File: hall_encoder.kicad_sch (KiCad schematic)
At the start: 30 parts, among them J1 Conn_02x03_Odd_Even, J2 Conn_01x04, J3 Conn_01x04, J4 Conn_01x02, J5 Conn_01x02, J6 Conn_01x02, SW1 RESET, U1 AP2210, U2 STM32F042F4Px, U3 MA730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

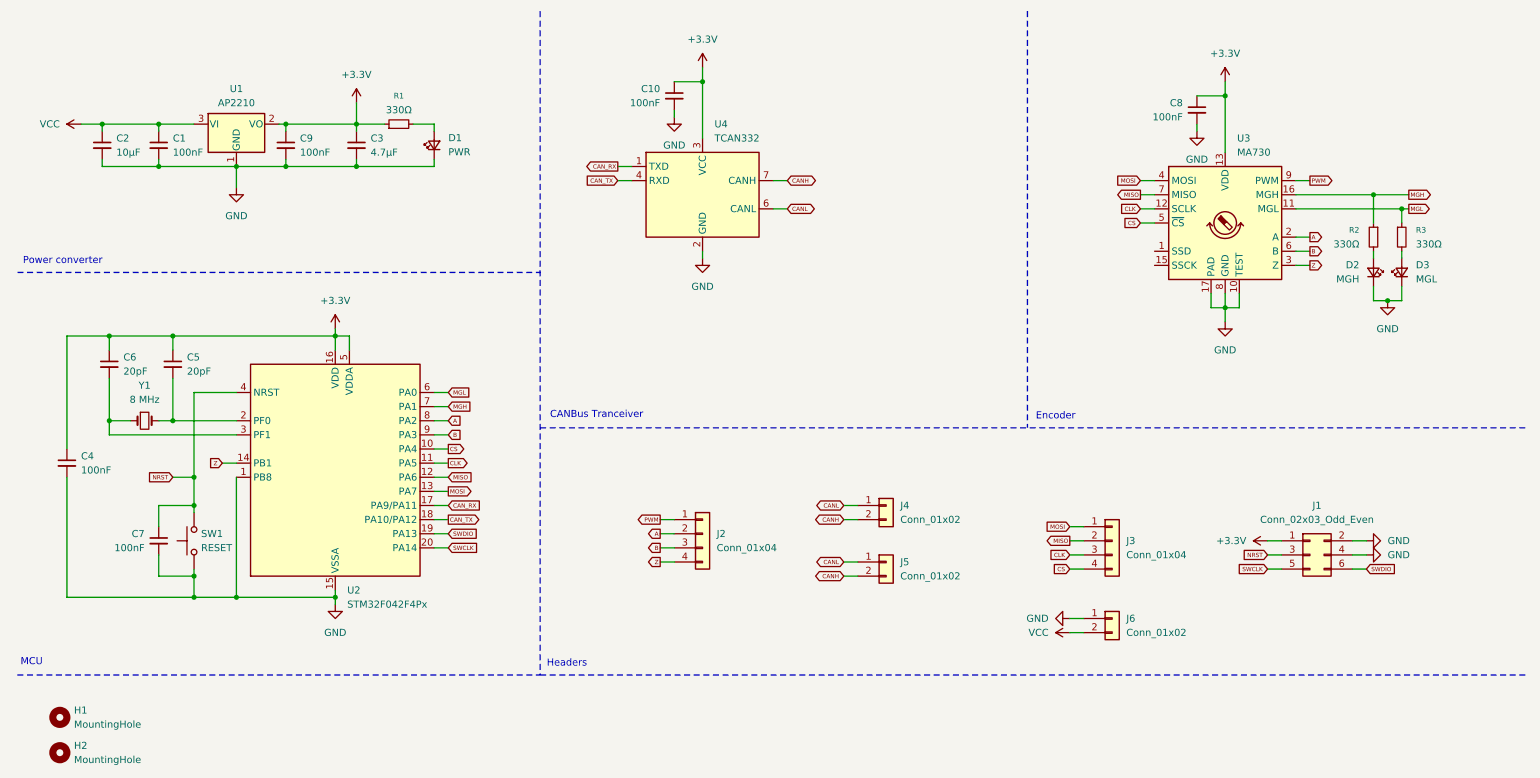
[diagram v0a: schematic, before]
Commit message: Remove all can components
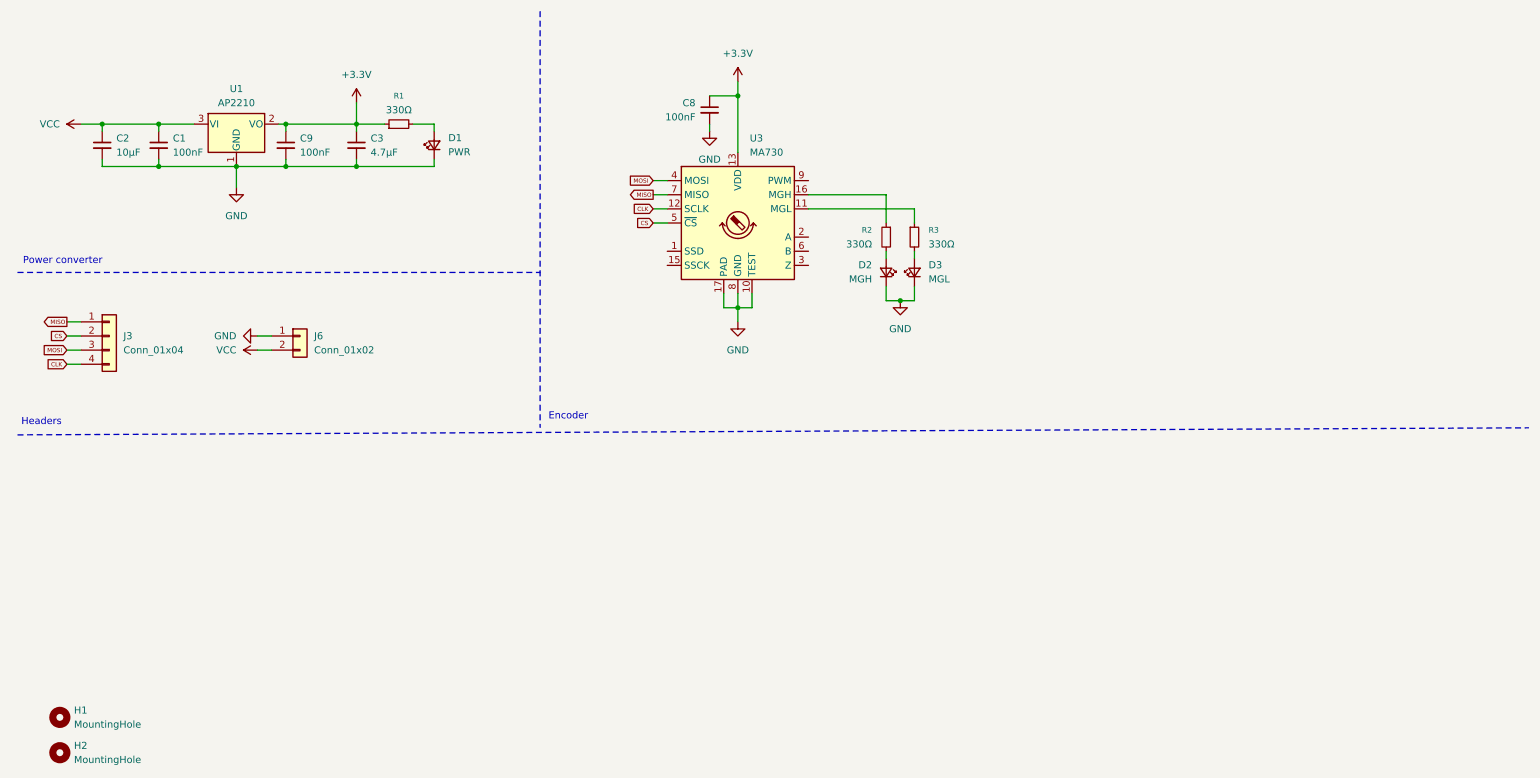
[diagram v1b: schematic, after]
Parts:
- removed C10, C4, C7: 100nF, Capacitor_SMD:C_0603_1608Metric_Pad1.08x0.95mm_HandSolder, symbol Device:C_Small
- removed C5, C6: 20pF, Capacitor_SMD:C_0603_1608Metric_Pad1.08x0.95mm_HandSolder, symbol Device:C_Small
- removed J1: Conn_02x03_Odd_Even, Connector_PinHeader_2.54mm:PinHeader_2x03_P2.54mm_Vertical, symbol Connector_Generic:Conn_02x03_Odd_Even
- removed J2: Conn_01x04, Connector_JST:JST_XH_B4B-XH-A_1x04_P2.50mm_Vertical, symbol Connector_Generic:Conn_01x04
- removed J4, J5: Conn_01x02, Connector_JST:JST_XH_B2B-XH-A_1x02_P2.50mm_Vertical, symbol Connector_Generic:Conn_01x02
- removed SW1: RESET, Button_Switch_SMD:SW_SPST_PTS810, symbol Switch:SW_Push
- removed U2: STM32F042F4Px, Package_SO:TSSOP-20_4.4x6.5mm_P0.65mm, symbol MCU_ST_STM32F0:STM32F042F4Px
- removed U4: TCAN332, Package_SO:PowerIntegrations_SO-8, symbol Interface_CAN_LIN:TCAN332
- removed Y1: 8 MHz, ECS-080-18-23G-JGN-TR:XTAL_ECS-23G_6P0X3P5X1P2_ECS-L, symbol Device:Crystal_Small
- J3: footprint Connector_JST:JST_XH_B4B-XH-A_1x04_P2.50mm_Vertical -> Connector_PinHeader_2.54mm:PinHeader_1x04_P2.54mm_Vertical
- J6: footprint Connector_JST:JST_XH_B2B-XH-A_1x02_P2.50mm_Vertical -> Connector_PinHeader_2.54mm:PinHeader_1x02_P2.54mm_Vertical
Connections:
- net CLK: now also J3.4 (Pin_4); no longer J3.3 (Pin_3)
- net CS: now also J3.2 (Pin_2); no longer J3.4 (Pin_4)
- net MISO: now also J3.1 (Pin_1); no longer J3.2 (Pin_2)
- net MOSI: now also J3.3 (Pin_3); no longer J3.1 (Pin_1)
- net A: no longer names the net of U3.2 (A)
- net B: no longer names the net of U3.6 (B)
- net MGH: no longer names the net of R2.1, U3.16 (MGH)
- net MGL: no longer names the net of R3.1, U3.11 (MGL)
- net PWM: no longer names the net of U3.9 (PWM)
- net Z: no longer names the net of U3.3 (Z)
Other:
- note removed: "CANBus Tranceiver"
- note removed: "MCU"
- moved on the sheet: C8, D2, D3, J3, J6, R2, R3, U3
